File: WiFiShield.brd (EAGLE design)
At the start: 68.6 x 53.3 mm, 37 parts, among them IC1 MC74VHCT50A, IC2 74AHC1G125, IC4 SPX3819M5-L-3-3, IC5 CC3000MOD, J10 Test, J2 Mode, J8 ARDUINO-SHIELD_R3, J9 U.FL-R-SMT-1(10)

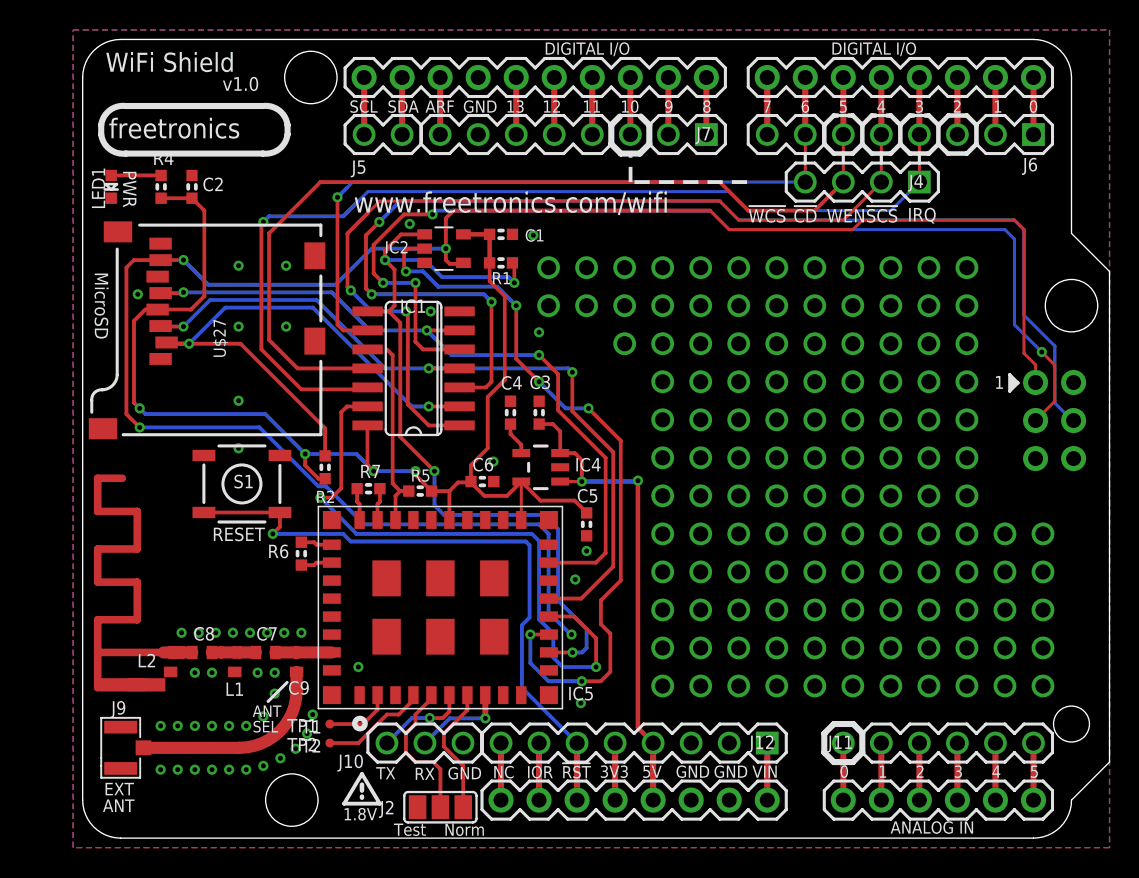
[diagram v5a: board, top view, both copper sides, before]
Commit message: Add silkscreen border
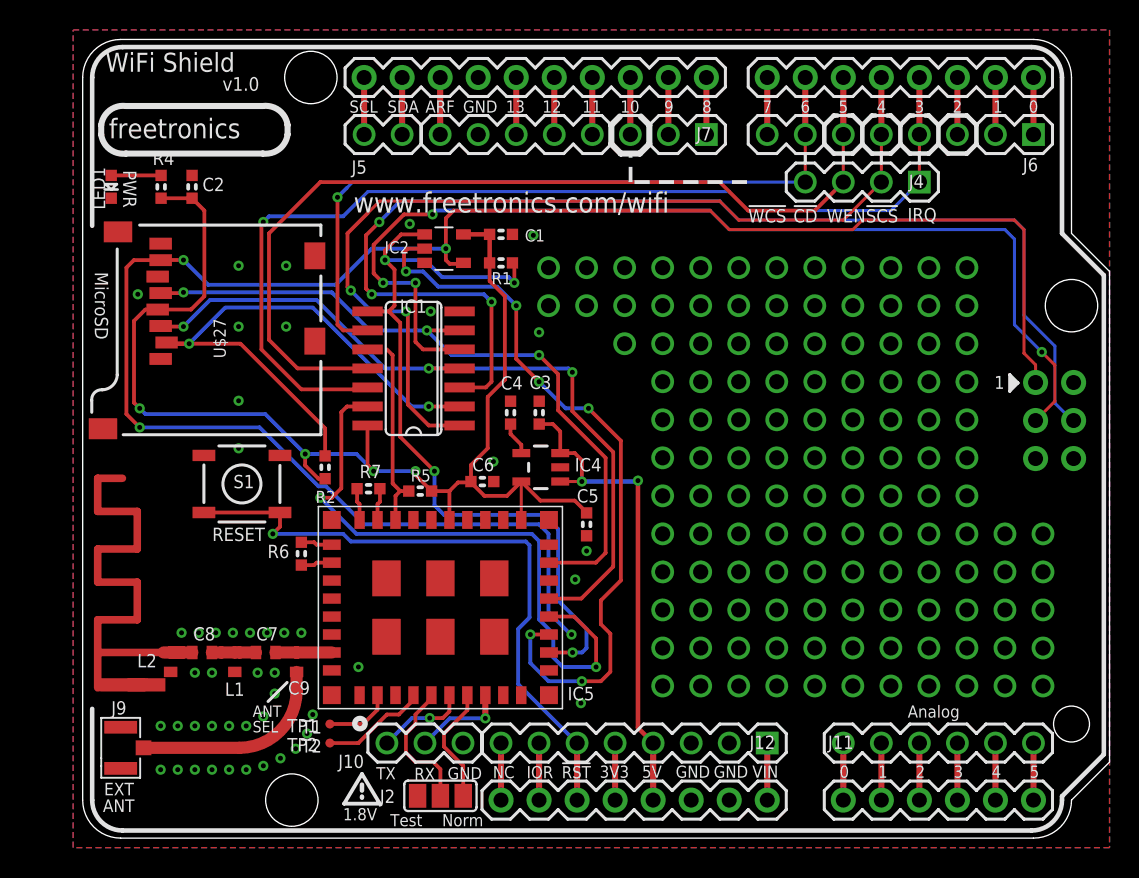
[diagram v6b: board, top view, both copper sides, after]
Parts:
- J8: device freetronics-luke:ARDUINO-SHIELD_R3 -> freetronics-angus:ARDUINO-SHIELD_R3
- moved J2 0.76 mm to (25.8, 2.83)
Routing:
- net WL_EN2: track 9.84 -> 9.08 mm
- net WL_EN1: track 8.66 -> 7.90 mm
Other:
- board text added: "Analog"
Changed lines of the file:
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@@
 <board>
 <plain>
-<text x="22.70125" y="0.15875" size="0.8128" layer="21" ratio="15">Test</text>
-<text x="26.035" y="0.15875" size="0.8128" layer="21" ratio="15">Norm</text>
+<text x="22.44725" y="0.79375" size="0.8128" layer="21" ratio="15">Test</text>
+<text x="25.908" y="0.79375" size="0.8128" layer="21" ratio="15">Norm</text>
 <text x="21.510625" y="3.9290625" size="0.8128" layer="21" ratio="15">TX</text>
 <text x="24.050625" y="3.889375" size="0.8128" layer="21" ratio="15">RX</text>
@@
 <text x="16.51" y="6.985" size="0.889" layer="21" ratio="15">T1</text>
 <text x="16.51" y="5.715" size="0.889" layer="21" ratio="15">T2</text>
-<wire x1="51.435" y1="5.715" x2="51.435" y2="6.985" width="0.4064" layer="21"/>
-<wire x1="51.435" y1="6.985" x2="52.07" y2="7.62" width="0.4064" layer="21"/>
-<wire x1="52.07" y1="7.62" x2="53.37175" y2="7.62" width="0.4064" layer="21"/>
-<wire x1="53.37175" y1="7.62" x2="53.975" y2="7.01675" width="0.4064" layer="21"/>
-<wire x1="53.975" y1="7.01675" x2="53.975" y2="5.715" width="0.4064" layer="21"/>
-<wire x1="53.975" y1="5.715" x2="53.34" y2="5.08" width="0.4064" layer="21"/>
-<wire x1="53.34" y1="5.08" x2="52.07" y2="5.08" width="0.4064" layer="21"/>
-<wire x1="52.07" y1="5.08" x2="51.435" y2="5.715" width="0.4064" layer="21"/>
 <wire x1="37.211" y1="46.355" x2="37.211" y2="47.625" width="0.4064" layer="21"/>
 <wire x1="37.211" y1="47.625" x2="37.7825" y2="48.1965" width="0.4064" layer="21"/>
@@
 <text x="13.255625" y="7.064375" size="0.762" layer="21" ratio="16">SEL</text>
 <text x="2.714625" y="37.81425" size="0.889" layer="21" ratio="16" rot="SR270">MicroSD</text>
+<wire x1="4.572" y1="0.508" x2="65.278" y2="0.508" width="0.3048" layer="21"/>
+<wire x1="65.278" y1="0.508" x2="67.31" y2="2.54" width="0.3048" layer="21" curve="90"/>
+<wire x1="67.31" y1="2.54" x2="67.31" y2="2.794" width="0.3048" layer="21"/>
+<wire x1="67.31" y1="2.794" x2="70.104" y2="5.588" width="0.3048" layer="21"/>
+<wire x1="70.104" y1="5.588" x2="70.104" y2="37.592" width="0.3048" layer="21"/>
+<wire x1="70.104" y1="37.592" x2="67.31" y2="40.386" width="0.3048" layer="21"/>
+<wire x1="67.31" y1="40.386" x2="67.31" y2="50.8" width="0.3048" layer="21"/>
+<wire x1="67.31" y1="50.8" x2="65.278" y2="52.832" width="0.3048" layer="21" curve="90"/>
+<wire x1="65.278" y1="52.832" x2="4.572" y2="52.832" width="0.3048" layer="21"/>
+<wire x1="4.572" y1="52.832" x2="2.54" y2="50.8" width="0.3048" layer="21" curve="90"/>
+<wire x1="2.54" y1="50.8" x2="2.54" y2="40.894" width="0.3048" layer="21"/>
+<wire x1="2.54" y1="8.636" x2="2.54" y2="2.54" width="0.3048" layer="21"/>
+<wire x1="2.54" y1="2.54" x2="4.572" y2="0.508" width="0.3048" layer="21" curve="90"/>
+<text x="57.007125" y="8.048625" size="0.8128" layer="21" ratio="15">Analog</text>
 </plain>
 <attributes>
@@
 <attribute name="VALUE" x="32.7152" y="30.025975" size="0.889" layer="27" font="vector" ratio="15" rot="R90"/>
 </element>
-<element name="J2" library="freetronics-master-v1" package="SJ_2" value="Mode" x="25.796875" y="2.06375" smashed="yes">
-<attribute name="NAME" x="21.74875" y="1.5875" size="0.889" layer="25" ratio="15"/>
+<element name="J2" library="freetronics-master-v1" package="SJ_2" value="Mode" x="25.796875" y="2.82575" smashed="yes">
+<attribute name="NAME" x="21.74875" y="2.3495" size="0.889" layer="25" ratio="15"/>
 </element>
 <element name="TP2" library="testpad" package="TP06R" value="R2" x="18.415" y="6.35" smashed="yes">
@@
 <attribute name="VALUE" x="10.8077" y="41.529" size="0.889" layer="27" font="vector" ratio="15" rot="R90"/>
 </element>
-<element name="J8" library="freetronics-luke" package="ARDUINO-SHIELD_R3" value="ARDUINO-SHIELD_R3" x="37.465" y="26.67" smashed="yes"/>
+<element name="J8" library="freetronics-angus" package="ARDUINO-SHIELD_R3" value="ARDUINO-SHIELD_R3" x="37.465" y="26.67" smashed="yes"/>
 <element name="J12" library="freetronics-master-v1" package="1X08" value="" x="47.625" y="6.35" smashed="yes" rot="R180">
 <attribute name="NAME" x="46.43755" y="5.9563" size="0.889" layer="25" ratio="15"/>
@@
 <via x="17.272" y="8.255" extent="1-16" drill="0.3302"/>
 <via x="5.588" y="36.322" extent="1-16" drill="0.3302"/>
+<via x="20.32" y="11.43" extent="1-16" drill="0.3302"/>
 </signal>
 <signal name="3V3">
@@
 <wire x1="24.13" y1="5.08" x2="25.320625" y2="5.08" width="0.254" layer="1"/>
 <wire x1="25.320625" y1="5.08" x2="25.796875" y2="4.60375" width="0.254" layer="1"/>
-<wire x1="25.796875" y1="4.60375" x2="25.796875" y2="2.06375" width="0.254" layer="1"/>
+<wire x1="25.796875" y1="4.60375" x2="25.796875" y2="2.82575" width="0.254" layer="1"/>
 </signal>
 <signal name="WL_EN1">
@@
 <wire x1="26.035" y1="6.985" x2="26.035" y2="6.111875" width="0.254" layer="1"/>
 <wire x1="26.035" y1="6.111875" x2="27.320875" y2="4.826" width="0.254" layer="1"/>
-<wire x1="27.320875" y1="2.06375" x2="27.320875" y2="4.826" width="0.254" layer="1"/>
+<wire x1="27.320875" y1="2.82575" x2="27.320875" y2="4.826" width="0.254" layer="1"/>
 </signal>
 <signal name="N$104">
@@
 <via x="14.605" y="20.32" extent="1-16" drill="0.3302"/>
 <wire x1="14.605" y1="20.32" x2="19.304" y2="20.32" width="0.254" layer="16"/>
-<wire x1="31.242" y1="10.033" x2="34.925" y2="6.35" width="0.254" layer="16"/>
+<wire x1="30.988" y1="10.287" x2="34.925" y2="6.35" width="0.254" layer="16"/>
 <wire x1="10.00125" y1="21.74875" x2="15.08125" y2="21.74875" width="0.254" layer="1"/>
 <wire x1="19.304" y1="20.32" x2="19.812" y2="19.812" width="0.254" layer="16"/>
 <wire x1="19.812" y1="19.812" x2="31.496" y2="19.812" width="0.254" layer="16"/>
-<wire x1="31.242" y1="14.224" x2="31.242" y2="10.033" width="0.254" layer="16"/>
 <wire x1="31.496" y1="19.812" x2="31.75" y2="19.558" width="0.254" layer="16"/>
 <wire x1="31.75" y1="19.558" x2="31.75" y2="14.732" width="0.254" layer="16"/>
-<wire x1="31.75" y1="14.732" x2="31.242" y2="14.224" width="0.254" layer="16"/>
+<wire x1="30.988" y1="10.287" x2="30.988" y2="13.97" width="0.254" layer="16"/>
+<wire x1="30.988" y1="13.97" x2="31.75" y2="14.732" width="0.254" layer="16"/>
 </signal>
 <signal name="IOREF">
@@
 <via x="66.04" y="10.16" extent="1-16" drill="1.016"/>
 </signal>
-<signal name="N$35">
-<via x="20.32" y="11.43" extent="1-16" drill="0.3302"/>
-</signal>
 </signals>

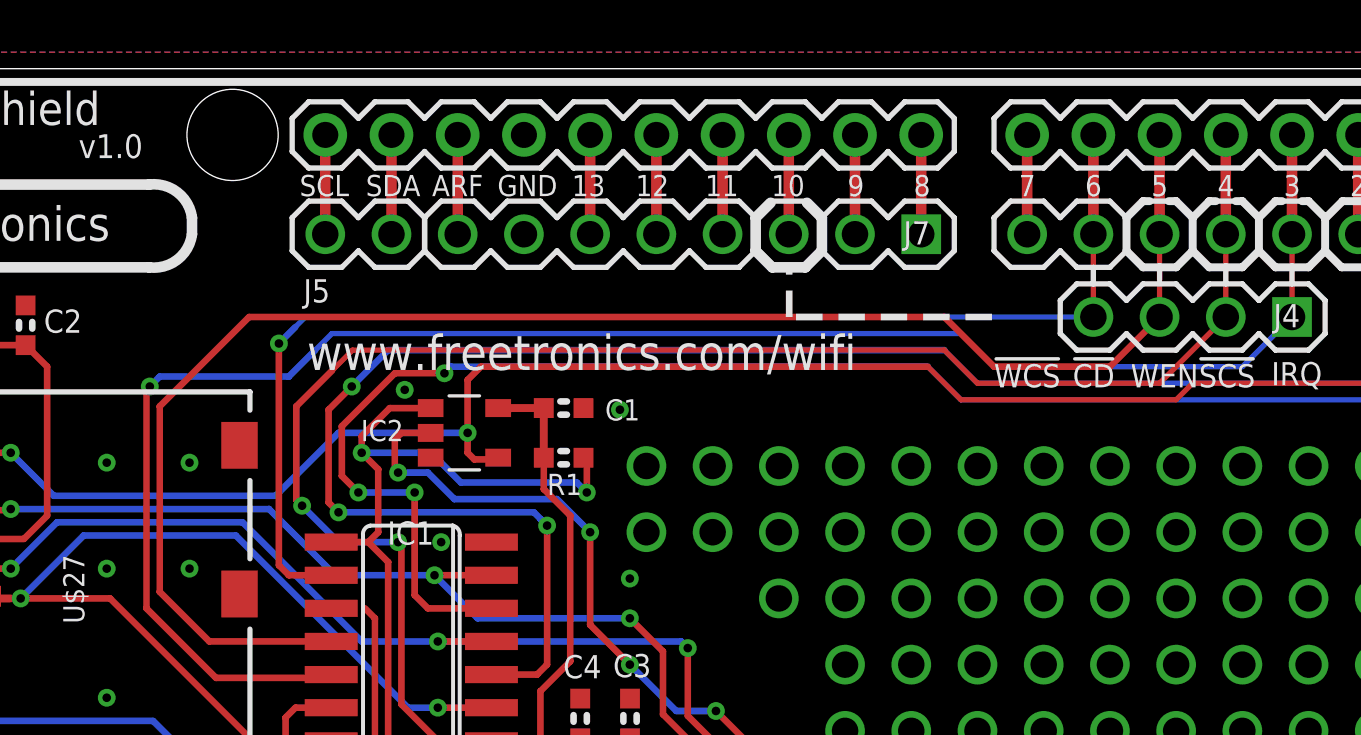
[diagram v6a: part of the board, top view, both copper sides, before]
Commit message: Update breakout/silkscreen to match 7f99dbe3f
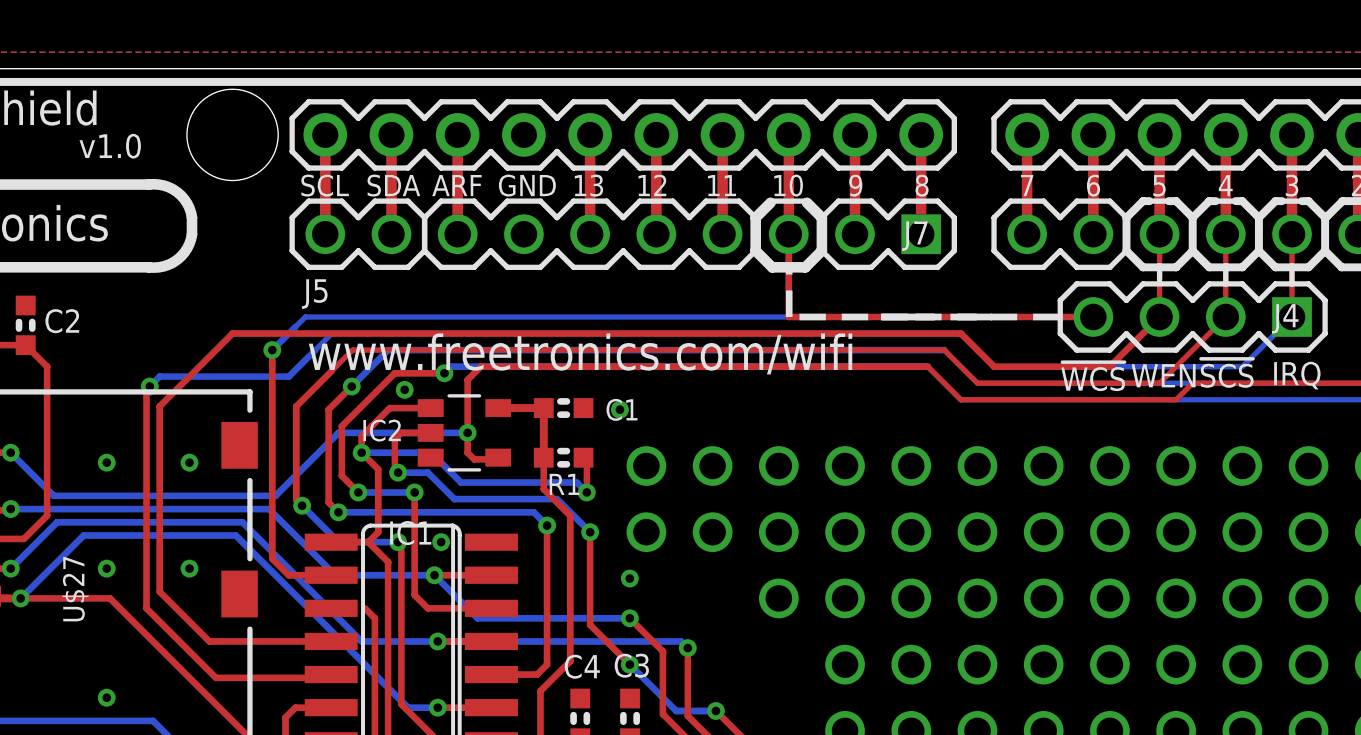
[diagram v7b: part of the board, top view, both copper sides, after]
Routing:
- net N$133: track 3.81 -> 19.4 mm
- net N$124: track 6.83 -> 3.81 mm
- net CC3000_EN_5V: track 58.8 -> 58.3 mm
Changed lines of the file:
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@@
 <setting verticaltext="up"/>
 </settings>
-<grid distance="10" unitdist="mil" unit="mil" style="lines" multiple="1" display="yes" altdistance="3.125" altunitdist="mil" altunit="mil"/>
+<grid distance="5" unitdist="mil" unit="mil" style="lines" multiple="1" display="yes" altdistance="3.125" altunitdist="mil" altunit="mil"/>
 <layers>
 <layer number="1" name="Top" color="4" fill="1" visible="yes" active="yes"/>
@@
 <vertex x="6.35" y="24.765"/>
 </polygon>
-<wire x1="46.275625" y1="43.815" x2="38.496875" y2="43.815" width="0.254" layer="21" style="dashdot"/>
+<wire x1="46.275625" y1="43.815" x2="46.228" y2="43.815" width="0.254" layer="21" style="dashdot"/>
+<wire x1="46.228" y1="43.815" x2="45.974" y2="43.815" width="0.254" layer="21" style="dashdot"/>
+<wire x1="45.974" y1="43.815" x2="43.053" y2="43.815" width="0.254" layer="21" style="dashdot"/>
+<wire x1="43.053" y1="43.815" x2="41.529" y2="43.815" width="0.254" layer="21" style="dashdot"/>
+<wire x1="41.529" y1="43.815" x2="38.496875" y2="43.815" width="0.254" layer="21" style="dashdot"/>
 <wire x1="38.496875" y1="43.815" x2="38.496875" y2="45.640625" width="0.254" layer="21" style="dashdot"/>
 <text x="56.99125" y="41.195625" size="0.889" layer="21" ratio="15">IRQ</text>
 <text x="54.213125" y="41.11625" size="0.889" layer="21" ratio="15">!SCS</text>
 <text x="51.59375" y="41.11625" size="0.889" layer="21" ratio="15">WEN</text>
-<text x="49.37125" y="41.11625" size="0.889" layer="21" ratio="15">!CD</text>
 <text x="10.556875" y="19.84375" size="0.889" layer="21" ratio="15">RESET</text>
 <wire x1="35.433" y1="44.2595" x2="23.241" y2="44.2595" width="0.3048" layer="22"/>
@@
 <text x="14.5415" y="51.181" size="1.27" layer="22" font="vector" ratio="17" rot="MR0">WiFi Shield</text>
 <text x="14.097" y="49.911" size="0.9144" layer="22" font="vector" ratio="15" rot="MR0">v1.0</text>
-<text x="46.355" y="41.11625" size="0.889" layer="21" ratio="15">!WCS</text>
+<text x="48.895" y="40.98925" size="0.889" layer="21" ratio="15">!WCS</text>
 <text x="48.656875" y="41.5925" size="0.889" layer="22" ratio="10" rot="MR0">!WCS</text>
 <text x="51.038125" y="41.5925" size="0.889" layer="22" ratio="10" rot="MR0">!CD</text>
@@
 <wire x1="20.558125" y1="2.69875" x2="20.558125" y2="2.778125" width="0.3048" layer="21"/>
 <wire x1="20.558125" y1="3.175" x2="20.558125" y2="3.571875" width="0.3048" layer="21"/>
-<wire x1="50.165" y1="45.72" x2="50.165" y2="45.085" width="0.2032" layer="21"/>
 <wire x1="52.705" y1="45.24375" x2="52.705" y2="45.72" width="0.2032" layer="21"/>
 <wire x1="55.245" y1="45.72" x2="55.245" y2="45.085" width="0.2032" layer="21"/>
@@
 <wire x1="2.54" y1="2.54" x2="4.572" y2="0.508" width="0.3048" layer="21" curve="90"/>
 <text x="57.007125" y="8.048625" size="0.8128" layer="21" ratio="15">Analog</text>
+<wire x1="46.228" y1="43.815" x2="48.895" y2="43.815" width="0.254" layer="21" style="longdash"/>
+<wire x1="43.053" y1="43.815" x2="41.529" y2="43.815" width="0.254" layer="21" style="longdash"/>
+<wire x1="43.053" y1="43.815" x2="45.974" y2="43.815" width="0.254" layer="21" style="longdash"/>
 </plain>
 <attributes>
@@
 <contactref element="J6" pad="7"/>
 <wire x1="50.165" y1="50.8" x2="50.165" y2="46.99" width="0.4064" layer="1"/>
-<wire x1="50.165" y1="43.97375" x2="50.165" y2="46.99" width="0.2032" layer="1"/>
 </signal>
 <signal name="N$125">
@@
 <contactref element="J7" pad="3"/>
 <contactref element="J8" pad="D10"/>
-<wire x1="38.481" y1="50.8" x2="38.481" y2="46.99" width="0.4064" layer="1"/>
+<wire x1="38.481" y1="50.8" x2="38.481" y2="47.117" width="0.4064" layer="1"/>
+<wire x1="38.481" y1="47.117" x2="38.481" y2="46.99" width="0.4064" layer="1"/>
+<wire x1="38.481" y1="47.117" x2="38.481" y2="43.815" width="0.254" layer="1"/>
+<wire x1="38.481" y1="43.815" x2="50.165" y2="43.815" width="0.254" layer="1"/>
+<wire x1="50.165" y1="43.815" x2="50.292" y2="43.815" width="0.254" layer="1"/>
+<wire x1="50.292" y1="43.815" x2="50.419" y2="43.942" width="0.254" layer="1"/>
+<wire x1="50.419" y1="43.942" x2="50.292" y2="43.942" width="0.254" layer="1"/>
+<wire x1="50.292" y1="43.942" x2="50.165" y2="43.815" width="0.254" layer="1"/>
 </signal>
 <signal name="N$134">
@@
 <wire x1="16.256" y1="31.369" x2="14.351" y2="33.274" width="0.254" layer="1"/>
 <wire x1="14.351" y1="33.274" x2="14.351" y2="40.386" width="0.254" layer="1"/>
-<wire x1="14.351" y1="40.386" x2="17.78" y2="43.815" width="0.254" layer="1"/>
 <wire x1="52.705" y1="43.815" x2="50.8" y2="41.91" width="0.254" layer="1"/>
 <wire x1="50.8" y1="41.91" x2="46.355" y2="41.91" width="0.254" layer="1"/>
-<wire x1="46.355" y1="41.91" x2="44.45" y2="43.815" width="0.254" layer="1"/>
-<wire x1="44.45" y1="43.815" x2="17.78" y2="43.815" width="0.254" layer="1"/>
+<wire x1="45.085" y1="43.18" x2="44.45" y2="43.815" width="0" layer="19" extent="1-16"/>
+<wire x1="14.351" y1="40.386" x2="17.145" y2="43.18" width="0.254" layer="1"/>
+<wire x1="17.145" y1="43.18" x2="45.085" y2="43.18" width="0.254" layer="1"/>
+<wire x1="45.085" y1="43.18" x2="46.355" y2="41.91" width="0.254" layer="1"/>
 </signal>
 <signal name="CC3000_EN_3V3">
@@
 <wire x1="19.558" y1="43.434" x2="19.939" y2="43.815" width="0.2032" layer="16"/>
 <wire x1="19.939" y1="43.815" x2="50.165" y2="43.815" width="0.2032" layer="16"/>
-<wire x1="19.558" y1="43.434" x2="18.923" y2="42.799" width="0.254" layer="16"/>
-<via x="18.923" y="42.799" extent="1-16" drill="0.3302"/>
-<wire x1="18.923" y1="42.799" x2="18.923" y2="34.29" width="0.254" layer="1"/>
-<wire x1="18.923" y1="34.29" x2="19.304" y2="33.909" width="0.254" layer="1"/>
+<wire x1="19.558" y1="43.434" x2="18.669" y2="42.545" width="0.254" layer="16"/>
+<via x="18.669" y="42.545" extent="1-16" drill="0.3302"/>
+<wire x1="18.669" y1="34.544" x2="19.304" y2="33.909" width="0.254" layer="1"/>
 <wire x1="19.304" y1="33.909" x2="20.9296" y2="33.909" width="0.254" layer="1"/>
+<wire x1="18.669" y1="42.545" x2="18.669" y2="34.544" width="0.254" layer="1"/>
 </signal>
 <signal name="CC3000_MISO">
